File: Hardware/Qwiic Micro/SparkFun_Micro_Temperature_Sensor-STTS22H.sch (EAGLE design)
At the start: 26 parts, among them J1 Qwiic Right Angle, U2 STTS22H

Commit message: Routes Micro, adds silk
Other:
- note added: "0 (GND)"
- note added: "1 (VDD)"
- note removed: "GND"
- note removed: "VDD"
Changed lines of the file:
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@@
 <wire x1="35.56" y1="83.82" x2="53.34" y2="83.82" width="0.1524" layer="97"/>
 <wire x1="53.34" y1="88.9" x2="73.66" y2="88.9" width="0.1524" layer="97"/>
-<text x="43.18" y="96.52" size="1.778" layer="97" font="vector" align="center">VDD</text>
-<text x="43.18" y="91.44" size="1.778" layer="97" font="vector" align="center">GND</text>
+<text x="43.18" y="96.52" size="1.778" layer="97" font="vector" align="center">1 (VDD)</text>
+<text x="43.18" y="91.44" size="1.778" layer="97" font="vector" align="center">0 (GND)</text>
 <text x="43.18" y="86.36" size="1.778" layer="97" font="vector" align="center">OPEN</text>
 <text x="63.5" y="86.36" size="1.778" layer="97" font="vector" align="center">Undefined</text>

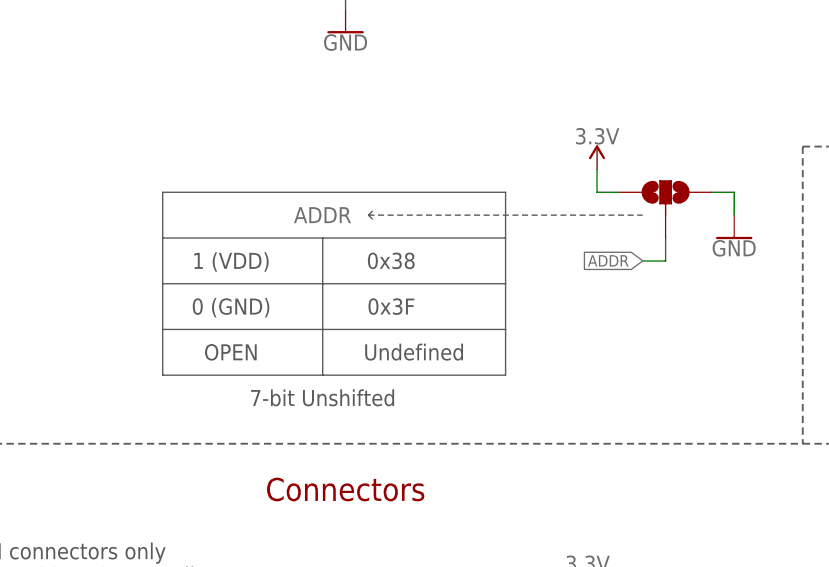
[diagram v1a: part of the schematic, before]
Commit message: Adds note for default addresses
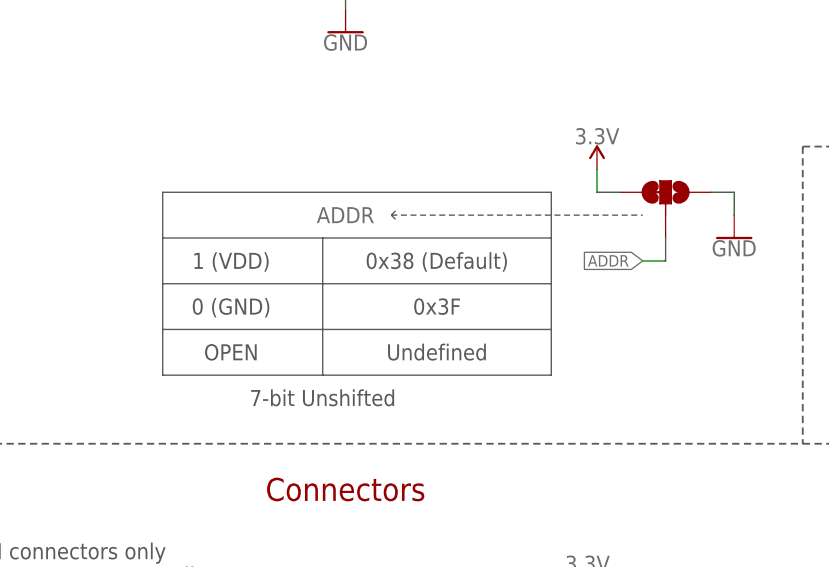
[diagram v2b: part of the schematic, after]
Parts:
- ADDR: value JUMPER-SMT_3_NO_SILK -> JUMPER-SMT_3_1-NC_TRACE_SILK; device SparkFun-Jumpers:JUMPER-SMT_3_NO_SILK -> SparkFun-Jumpers:JUMPER-SMT_3_1-NC_TRACE_SILK
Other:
- note added: "0x38 (Default)"
- note removed: "0x38"
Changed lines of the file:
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@@
 <part name="R3" library="SparkFun-Resistors" deviceset="10KOHM" device="-0402T-1/16W-1%" value="10k"/>
 <part name="SUPPLY5" library="SparkFun-PowerSymbols" deviceset="3.3V" device=""/>
-<part name="ADDR" library="SparkFun-Jumpers" deviceset="JUMPER-SMT_3_NO" device="_SILK" package3d_urn="urn:adsk.eagle:package:39285/1"/>
+<part name="ADDR" library="SparkFun-Jumpers" deviceset="JUMPER-SMT_3_1-NC_TRACE" device="_SILK" package3d_urn="urn:adsk.eagle:package:39288/1"/>
 <part name="SUPPLY8" library="SparkFun-PowerSymbols" deviceset="3.3V" device=""/>
 <part name="GND5" library="SparkFun-PowerSymbols" deviceset="GND" device=""/>
@@
 <wire x1="35.56" y1="93.98" x2="35.56" y2="88.9" width="0.1524" layer="97"/>
 <wire x1="35.56" y1="88.9" x2="35.56" y2="83.82" width="0.1524" layer="97"/>
-<wire x1="53.34" y1="83.82" x2="73.66" y2="83.82" width="0.1524" layer="97"/>
-<wire x1="73.66" y1="83.82" x2="73.66" y2="88.9" width="0.1524" layer="97"/>
-<wire x1="73.66" y1="88.9" x2="73.66" y2="93.98" width="0.1524" layer="97"/>
-<wire x1="73.66" y1="93.98" x2="73.66" y2="99.06" width="0.1524" layer="97"/>
-<wire x1="73.66" y1="99.06" x2="73.66" y2="104.14" width="0.1524" layer="97"/>
-<wire x1="73.66" y1="104.14" x2="35.56" y2="104.14" width="0.1524" layer="97"/>
+<wire x1="53.34" y1="83.82" x2="78.74" y2="83.82" width="0.1524" layer="97"/>
+<wire x1="78.74" y1="83.82" x2="78.74" y2="88.9" width="0.1524" layer="97"/>
+<wire x1="78.74" y1="88.9" x2="78.74" y2="93.98" width="0.1524" layer="97"/>
+<wire x1="78.74" y1="93.98" x2="78.74" y2="99.06" width="0.1524" layer="97"/>
+<wire x1="78.74" y1="99.06" x2="78.74" y2="104.14" width="0.1524" layer="97"/>
+<wire x1="78.74" y1="104.14" x2="35.56" y2="104.14" width="0.1524" layer="97"/>
 <wire x1="35.56" y1="99.06" x2="53.34" y2="99.06" width="0.1524" layer="97"/>
-<wire x1="53.34" y1="99.06" x2="73.66" y2="99.06" width="0.1524" layer="97"/>
+<wire x1="53.34" y1="99.06" x2="78.74" y2="99.06" width="0.1524" layer="97"/>
 <wire x1="53.34" y1="99.06" x2="53.34" y2="93.98" width="0.1524" layer="97"/>
 <wire x1="53.34" y1="93.98" x2="53.34" y2="88.9" width="0.1524" layer="97"/>
@@
 <wire x1="35.56" y1="88.9" x2="53.34" y2="88.9" width="0.1524" layer="97"/>
 <wire x1="35.56" y1="83.82" x2="53.34" y2="83.82" width="0.1524" layer="97"/>
-<wire x1="53.34" y1="88.9" x2="73.66" y2="88.9" width="0.1524" layer="97"/>
+<wire x1="53.34" y1="88.9" x2="78.74" y2="88.9" width="0.1524" layer="97"/>
 <text x="43.18" y="96.52" size="1.778" layer="97" font="vector" align="center">1 (VDD)</text>
 <text x="43.18" y="91.44" size="1.778" layer="97" font="vector" align="center">0 (GND)</text>
 <text x="43.18" y="86.36" size="1.778" layer="97" font="vector" align="center">OPEN</text>
-<text x="63.5" y="86.36" size="1.778" layer="97" font="vector" align="center">Undefined</text>
+<text x="66.04" y="86.36" size="1.778" layer="97" font="vector" align="center">Undefined</text>
 <text x="53.34" y="81.28" size="1.778" layer="97" font="vector" align="center">7-bit Unshifted</text>
 <wire x1="35.56" y1="93.98" x2="53.34" y2="93.98" width="0.1524" layer="97"/>
-<wire x1="53.34" y1="93.98" x2="73.66" y2="93.98" width="0.1524" layer="97"/>
-<text x="60.96" y="96.52" size="1.778" layer="97" font="vector" align="center">0x38</text>
-<text x="60.96" y="91.44" size="1.778" layer="97" font="vector" align="center">0x3F</text>
-<wire x1="58.42" y1="101.6" x2="88.9" y2="101.6" width="0.1524" layer="97" style="dashdot"/>
-<wire x1="58.42" y1="101.6" x2="59.182" y2="102.362" width="0.1524" layer="97" style="dashdot"/>
-<wire x1="58.42" y1="101.6" x2="59.182" y2="100.838" width="0.1524" layer="97" style="dashdot"/>
+<wire x1="53.34" y1="93.98" x2="78.74" y2="93.98" width="0.1524" layer="97"/>
+<text x="66.04" y="96.52" size="1.778" layer="97" font="vector" align="center">0x38 (Default)</text>
+<text x="66.04" y="91.44" size="1.778" layer="97" font="vector" align="center">0x3F</text>
+<wire x1="60.96" y1="101.6" x2="88.9" y2="101.6" width="0.1524" layer="97" style="dashdot"/>
+<wire x1="60.96" y1="101.6" x2="61.722" y2="102.362" width="0.1524" layer="97" style="dashdot"/>
+<wire x1="60.96" y1="101.6" x2="61.722" y2="100.838" width="0.1524" layer="97" style="dashdot"/>
 <text x="68.58" y="177.8" size="2.54" layer="94" font="vector" align="center">Temperature Sensor - STTS22H</text>
 </plain>
@@
 </instance>
 <instance part="ADDR" gate="G$1" x="91.44" y="104.14" smashed="yes" rot="MR90">
-<attribute name="NAME" x="53.34" y="101.6" size="1.778" layer="95" font="vector" rot="MR0" align="center"/>
+<attribute name="NAME" x="55.88" y="101.6" size="1.778" layer="95" font="vector" rot="MR0" align="center"/>
 </instance>
 <instance part="SUPPLY8" gate="G$1" x="83.82" y="106.68" smashed="yes">

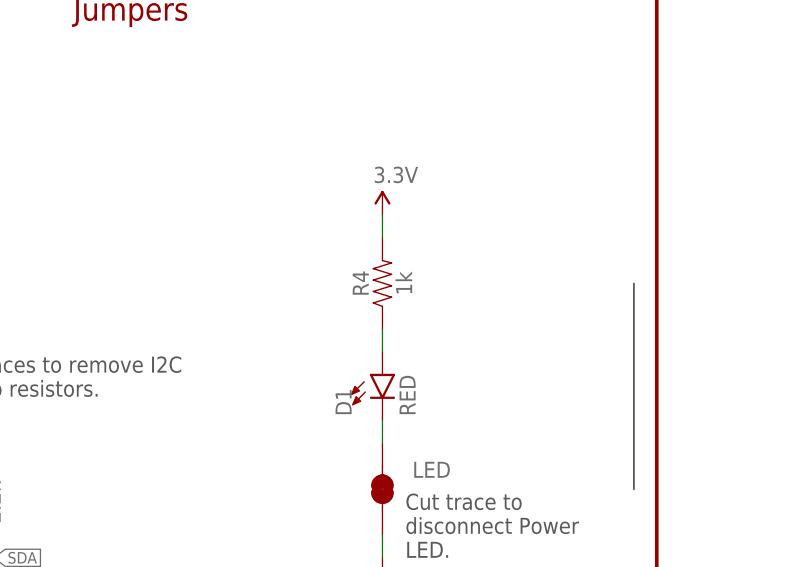
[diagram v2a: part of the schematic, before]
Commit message: Fixes off center footprint, adds center pad on temp sensor to ground
*
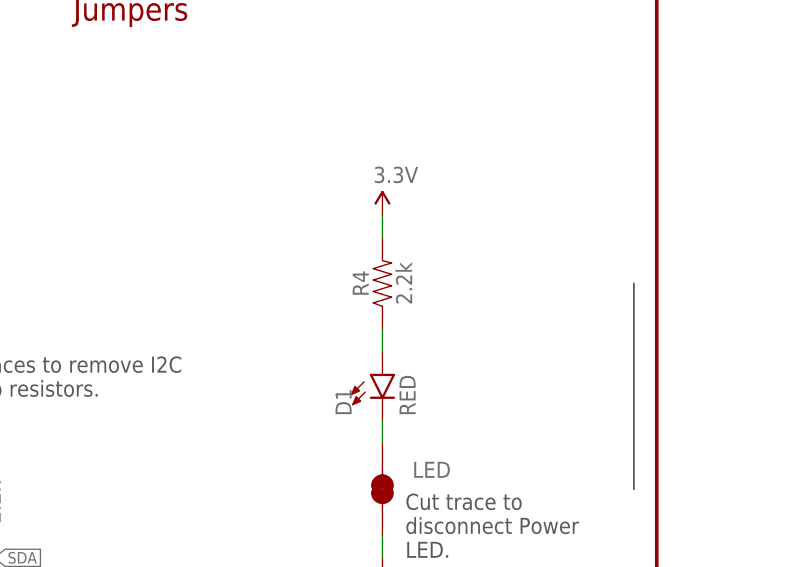
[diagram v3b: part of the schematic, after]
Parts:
- R4: value 1k -> 2.2k; device SparkFun-Resistors:1KOHM-0402T-1/16W-1% -> SparkFun-Resistors:2.2KOHM-0402T-1/16W-1%
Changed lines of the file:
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@@
 <part name="FD2" library="SparkFun-Aesthetics" deviceset="FIDUCIAL" device="UFIDUCIAL"/>
 <part name="D1" library="SparkFun-LED" deviceset="LED-RED" device="_0402" value="RED"/>
-<part name="R4" library="SparkFun-Resistors" deviceset="1KOHM" device="-0402T-1/16W-1%" value="1k"/>
+<part name="R4" library="SparkFun-Resistors" deviceset="2.2KOHM" device="-0402T-1/16W-1%" value="2.2k"/>
 <part name="LED" library="SparkFun-Jumpers" deviceset="JUMPER-SMT_2_NC_TRACE" device="_SILK" package3d_urn="urn:adsk.eagle:package:39281/1"/>
 <part name="SUPPLY3" library="SparkFun-PowerSymbols" deviceset="3.3V" device=""/>
